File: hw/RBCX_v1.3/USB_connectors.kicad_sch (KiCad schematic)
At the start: 13 parts, among them J49 Conn_01x04, J50 Conn_01x04, U21 USB_C

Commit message: Production files
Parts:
- J49, J50: JLCPCB_CORRECTION (none) -> 0;-3.81;90
- TP58: JLCPCB_IGNORE (none) -> 1
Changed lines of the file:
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@@
+      (effects (font (size 1.27 1.27)) hide)
+    )
+    (property "JLCPCB_CORRECTION" "0;-3.81;90" (id 6) (at 152.4 109.22 0)
       (effects (font (size 1.27 1.27)) hide)
     )
@@
       (effects (font (size 1.27 1.27)) hide)
     )
+    (property "JLCPCB_CORRECTION" "0;-3.81;90" (id 6) (at 172.72 143.51 0)
+      (effects (font (size 1.27 1.27)) hide)
+    )
     (pin "1")
     (pin "2")
@@
       (effects (font (size 1.27 1.27)) hide)
     )
+    (property "JLCPCB_IGNORE" "1" (id 4) (at 134.62 135.89 0)
+      (effects (font (size 1.27 1.27)) hide)
+    )

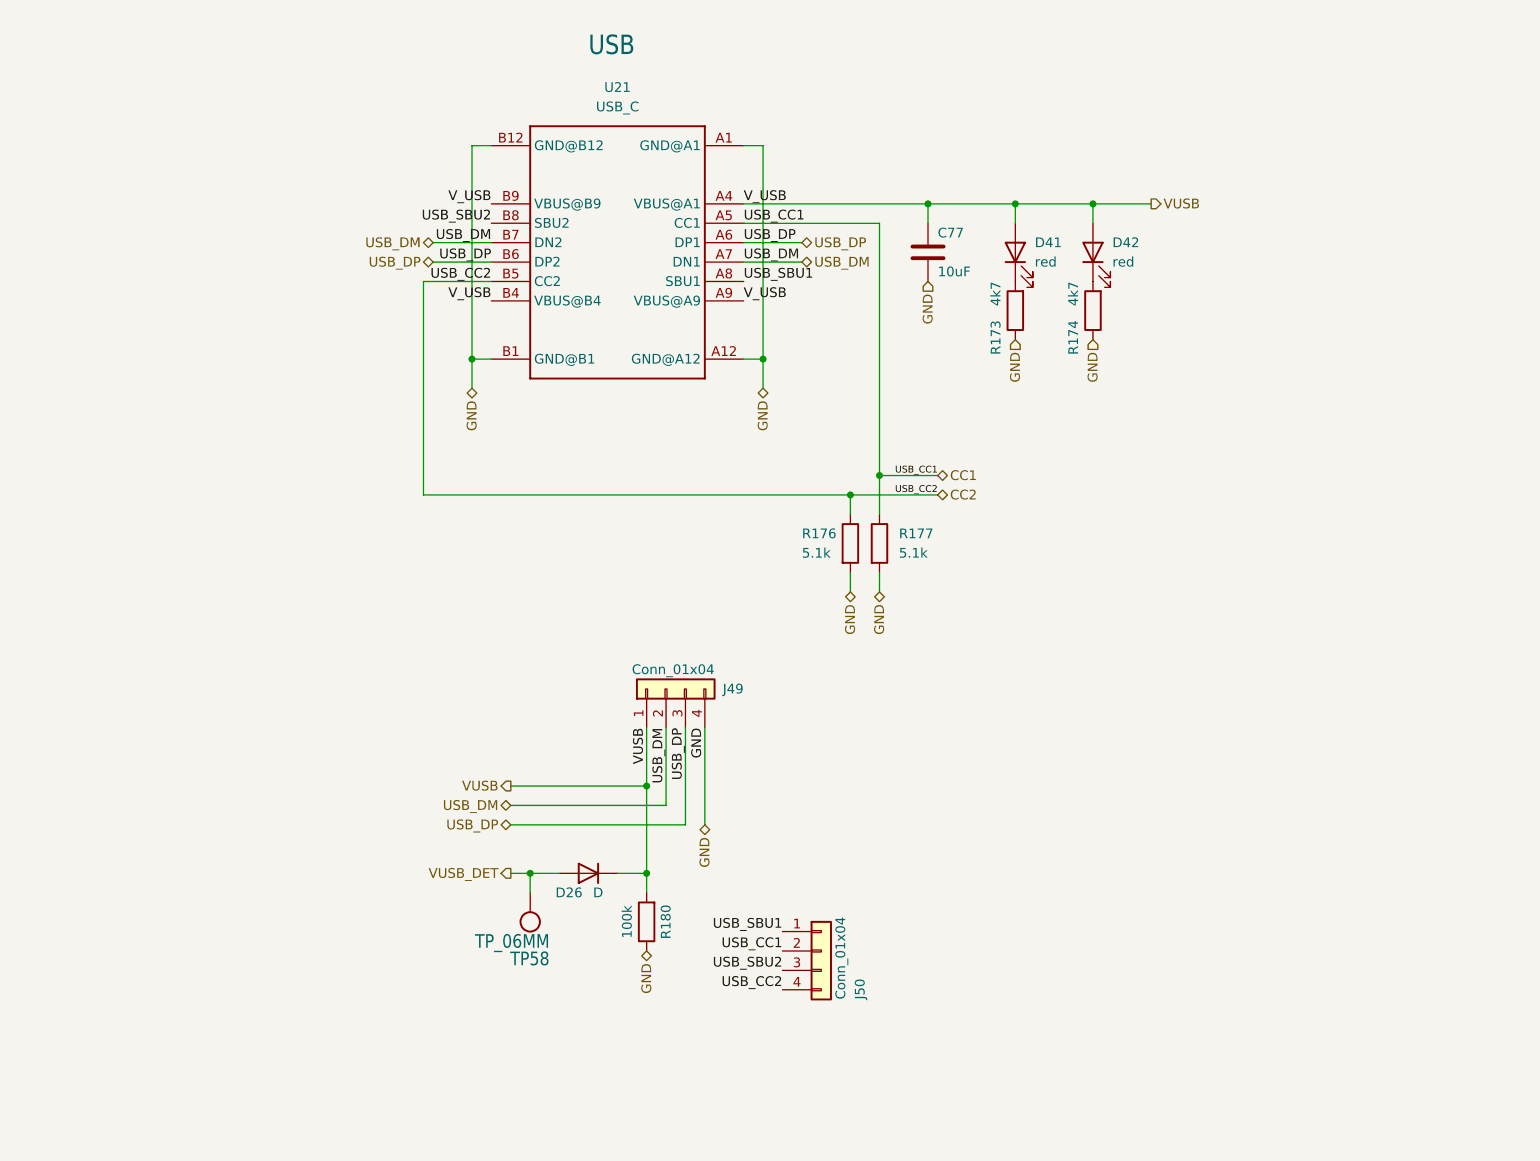
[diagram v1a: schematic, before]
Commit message: Kuba issues
Change of power transistor from JSM3622 to JMSL0302AU

NTC connectors

Moving the Cell balancer behind the switch

and some little things
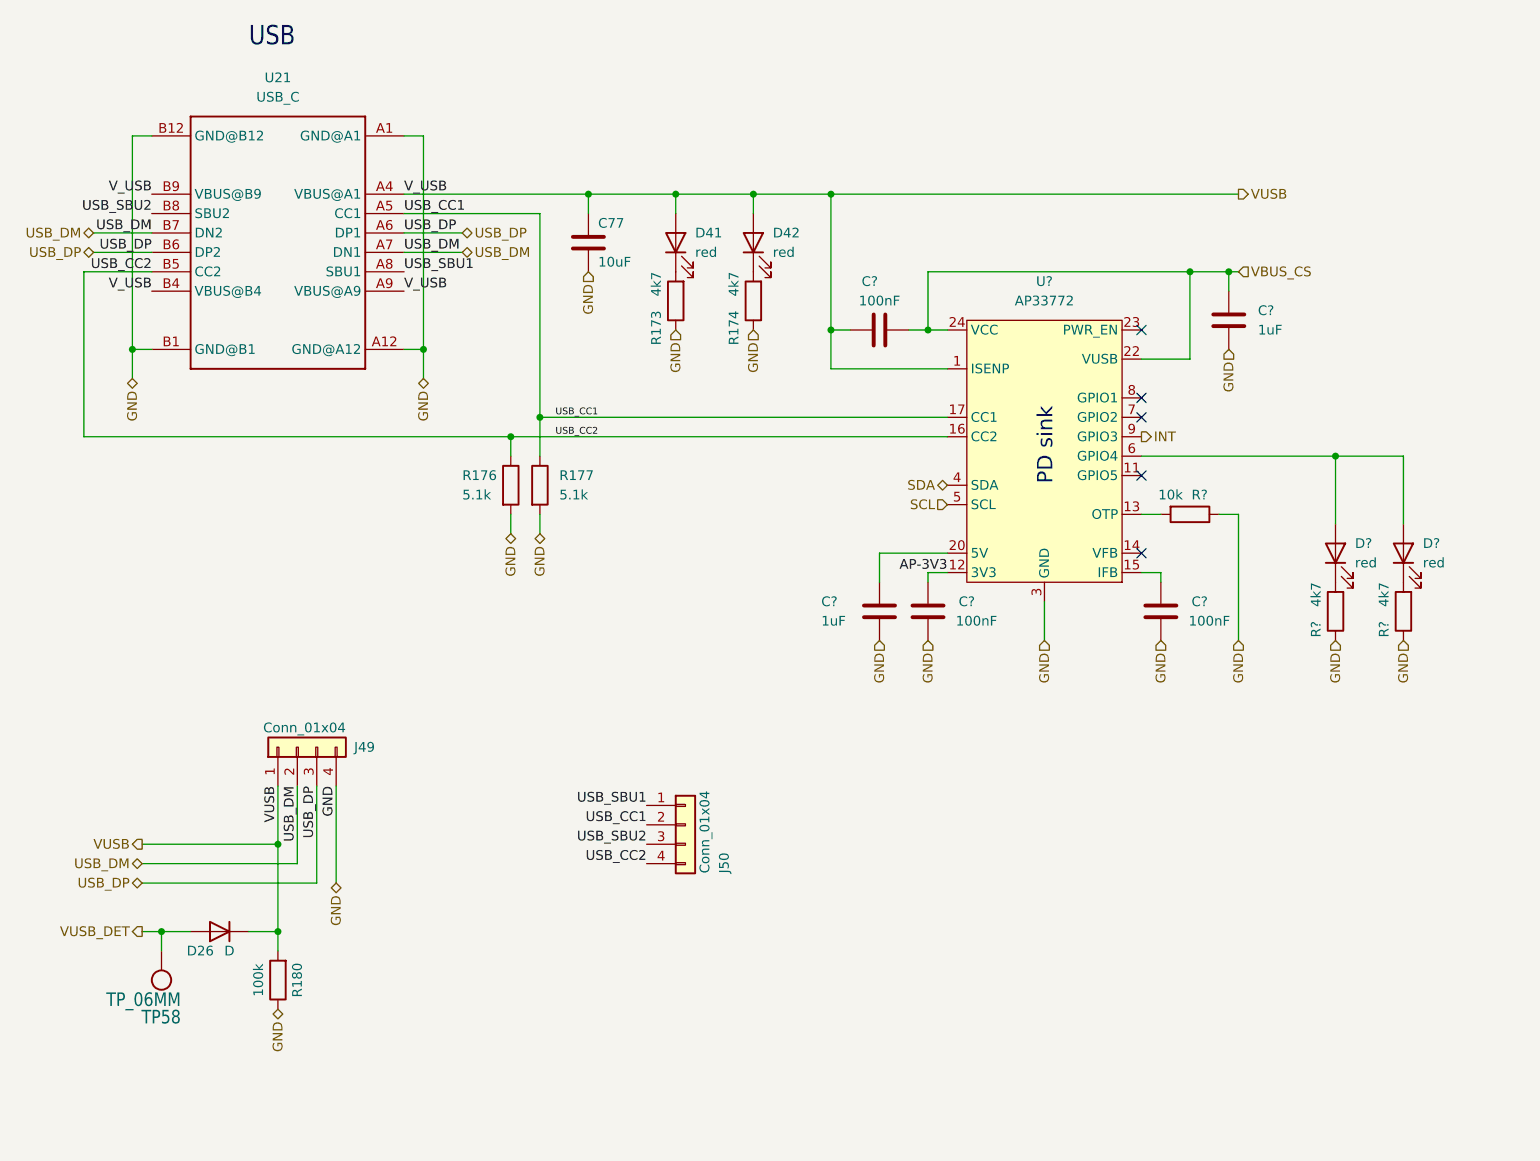
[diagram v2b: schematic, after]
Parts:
- added C? (x2): 1uF, Resistor_SMD:R_0402_1005Metric, symbol Device:C
- added C? (x3): 100nF, Capacitor_SMD:C_0402_1005Metric, symbol Device:C
- added D? (x2): red, LED_SMD:LED_0603_1608Metric, symbol Device:LED
- added R?: 10k, Capacitor_SMD:C_0201_0603Metric, symbol Device:R
- added R? (x2): 4k7, Resistor_SMD:R_0201_0603Metric, symbol Device:R
- added U?: AP33772, Package_DFN_QFN:QFN-24-1EP_4x4mm_P0.5mm_EP2.6x2.6mm, symbol RBCX:AP33772
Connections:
- net GND: now also C?.1, C?.1, C?.2, C?.2, R?.1, R?.1, R?.1, U?.25 (GND), U?.3 (GND)
- net VUSB: now also C?.1, U?.1 (ISENP)
- net CC1 renamed USB_CC1
- net USB_CC1: now also U?.17 (CC1)
- net CC2 renamed USB_CC2
- net USB_CC2: now also U?.16 (CC2)
- new net: R?.2, U?.13 (OTP)
- new net: C?.2, U?.15 (IFB)
- new net: C?.1, U?.20 (5V)
- new net: D?.2 (A), D?.2 (A), U?.6 (GPIO4)
- new net: D?.1 (K), R?.2 (x2)
- new net AP-3V3: C?.2, U?.12 (3V3)
- new net INT: U?.9 (GPIO3)
- new net SCL: U?.5 (SCL)
- new net SDA: U?.4 (SDA)
- new net VBUS_CS: C?.1, C?.2, U?.22 (VUSB), U?.24 (VCC)
- no-connect marks 0 -> 5
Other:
- note added: "PD sink"
- moved on the sheet: C77, D26, D41, D42, J49, J50, R173, R174, R176, R177, R180, TP58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

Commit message: Kuba issues - PCB
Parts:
- gave numbers to parts that had none: 11
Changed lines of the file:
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@@
   (symbol (lib_id "Device:R") (at 220.98 86.36 270) (unit 1)
     (in_bom yes) (on_board yes)
-    (property "Reference" "R?" (id 0) (at 222.25 83.82 90))
+    (property "Reference" "R172" (id 0) (at 222.25 83.82 90))
     (property "Value" "10k" (id 1) (at 218.44 83.82 90))
     (property "Footprint" "Capacitor_SMD:C_0201_0603Metric" (id 2) (at 220.98 84.582 90)
@@
   (symbol (lib_id "RBCX:AP33772") (at 201.93 62.23 0) (unit 1)
     (in_bom yes) (on_board yes) (fields_autoplaced)
-    (property "Reference" "U?" (id 0) (at 201.93 55.88 0))
+    (property "Reference" "U22" (id 0) (at 201.93 55.88 0))
     (property "Value" "AP33772" (id 1) (at 201.93 58.42 0))
     (property "Footprint" "Package_DFN_QFN:QFN-24-1EP_4x4mm_P0.5mm_EP2.6x2.6mm" (id 2) (at 201.93 62.23 0)
@@
   (symbol (lib_id "Device:LED") (at 248.92 91.44 90) (unit 1)
     (in_bom yes) (on_board yes)
-    (property "Reference" "D?" (id 0) (at 251.46 90.17 90)
+    (property "Reference" "D44" (id 0) (at 251.46 90.17 90)
       (effects (font (size 1.27 1.27)) (justify right))
     )
@@
   (symbol (lib_id "Device:R") (at 240.03 99.06 180) (unit 1)
     (in_bom yes) (on_board yes)
-    (property "Reference" "R?" (id 0) (at 237.49 100.33 90)
+    (property "Reference" "R175" (id 0) (at 237.49 100.33 90)
       (effects (font (size 1.27 1.27)) (justify left))
     )
@@
   (symbol (lib_id "Device:C") (at 180.34 99.06 0) (unit 1)
     (in_bom yes) (on_board yes)
-    (property "Reference" "C?" (id 0) (at 172.72 97.79 0)
+    (property "Reference" "C80" (id 0) (at 172.72 97.79 0)
       (effects (font (size 1.27 1.27)) (justify left))
     )
@@
   (symbol (lib_id "Device:C") (at 180.34 62.23 90) (unit 1)
     (in_bom yes) (on_board yes)
-    (property "Reference" "C?" (id 0) (at 179.07 55.88 90))
+    (property "Reference" "C79" (id 0) (at 179.07 55.88 90))
     (property "Value" "100nF" (id 1) (at 180.34 58.42 90))
     (property "Footprint" "Capacitor_SMD:C_0402_1005Metric" (id 2) (at 184.15 61.2648 0)
@@
   (symbol (lib_id "Device:C") (at 217.17 99.06 180) (unit 1)
     (in_bom yes) (on_board yes)
-    (property "Reference" "C?" (id 0) (at 222.25 97.79 0))
+    (property "Reference" "C82" (id 0) (at 222.25 97.79 0))
     (property "Value" "100nF" (id 1) (at 223.52 100.33 0))
     (property "Footprint" "Capacitor_SMD:C_0402_1005Metric" (id 2) (at 216.2048 95.25 0)
@@
   (symbol (lib_id "Device:R") (at 248.92 99.06 180) (unit 1)
     (in_bom yes) (on_board yes)
-    (property "Reference" "R?" (id 0) (at 246.38 100.33 90)
+    (property "Reference" "R178" (id 0) (at 246.38 100.33 90)
       (effects (font (size 1.27 1.27)) (justify left))
     )
@@
   (symbol (lib_id "Device:C") (at 226.06 60.96 0) (unit 1)
     (in_bom yes) (on_board yes) (fields_autoplaced)
-    (property "Reference" "C?" (id 0) (at 229.87 59.6899 0)
+    (property "Reference" "C78" (id 0) (at 229.87 59.6899 0)
       (effects (font (size 1.27 1.27)) (justify left))
     )
@@
   (symbol (lib_id "Device:C") (at 186.69 99.06 180) (unit 1)
     (in_bom yes) (on_board yes)
-    (property "Reference" "C?" (id 0) (at 191.77 97.79 0))
+    (property "Reference" "C81" (id 0) (at 191.77 97.79 0))
     (property "Value" "100nF" (id 1) (at 193.04 100.33 0))
     (property "Footprint" "Capacitor_SMD:C_0402_1005Metric" (id 2) (at 185.7248 95.25 0)
@@
   (symbol (lib_id "Device:LED") (at 240.03 91.44 90) (unit 1)
     (in_bom yes) (on_board yes)
-    (property "Reference" "D?" (id 0) (at 242.57 90.17 90)
+    (property "Reference" "D43" (id 0) (at 242.57 90.17 90)
       (effects (font (size 1.27 1.27)) (justify right))
     )
